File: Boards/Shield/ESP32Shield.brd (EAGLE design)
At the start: 58.4 x 25.4 mm, 28 parts, among them Q1 220mA/50V/3.5Ω, U1 5V

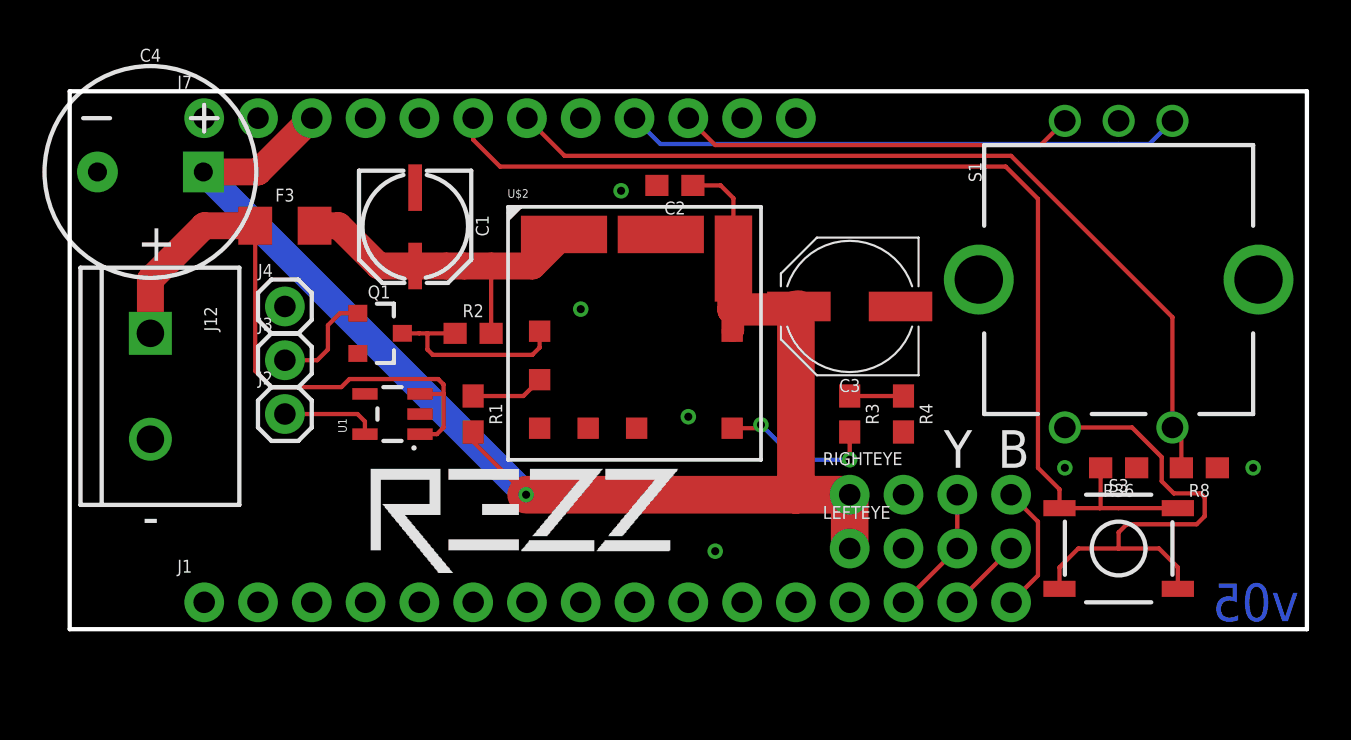
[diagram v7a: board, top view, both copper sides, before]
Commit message: updating board to V06, finangling code to work with WROOM
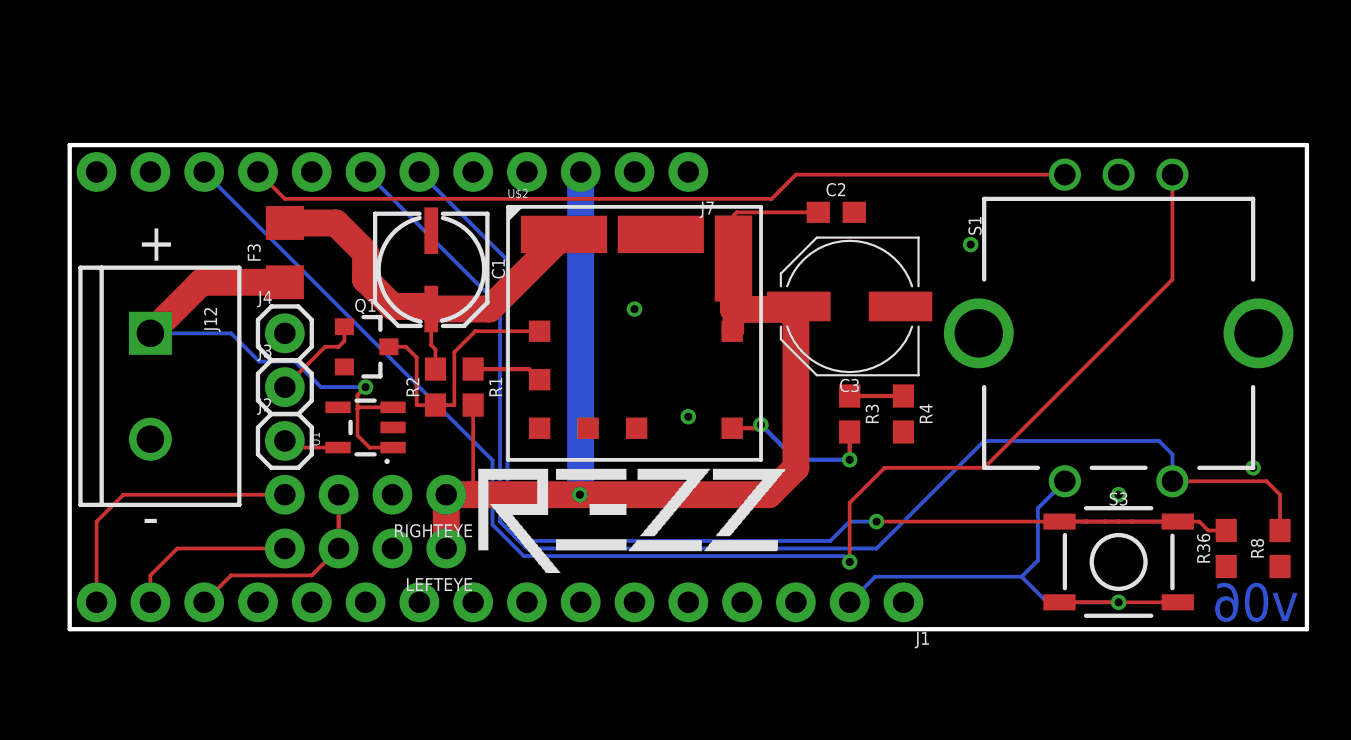
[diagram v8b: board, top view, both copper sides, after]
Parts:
- removed C4: 1mF, SparkFun-Capacitors:CPOL-RADIAL-5MM-10MM
- moved J1 33.0 mm to (39.4, 1.27), turned to 180 degrees
- moved J7 23.0 mm to (29.2, 21.6), turned to 180 degrees
- moved LEFTEYE 19.0 mm to (17.8, 3.81), turned to 180 degrees
- moved RIGHTEYE 19.0 mm to (17.8, 6.35), turned to 180 degrees
- moved C2 7.73 mm to (36.2, 19.7), turned to 0 degrees
- moved R36 6.35 mm to (54.6, 3.81), turned to 90 degrees
- moved R8 5.39 mm to (57.1, 3.81), turned to 90 degrees
- moved U$1 5.08 mm to (26.6, 5.11)
- moved R2 3.10 mm to (17.3, 11.4), turned to 90 degrees
- moved U$4 2.79 mm to (49.5, 17.7)
- moved S1 2.54 mm to (49.5, 14.0)
- moved U$3 2.54 mm to (49.4, 9.91)
- moved C1 2.17 mm to (17.3, 17.0)
- moved U1 1.42 mm to (14.0, 9.53)
- moved F3 1.27 mm to (10.2, 17.8), turned to 90 degrees
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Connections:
- removed net 14/ENC-B: J7.10, S1.B
- removed net 32/ENC-A: J7.9, S1.A
- removed net 3V3: J1.2
- new net 14/ENC-A: J7.10, S1.A
- new net 32/ENC-B: J7.9, S1.B
- net 3.3V: now also J1.2
- net 5V: no longer C4.+
- net GND: no longer C4.-
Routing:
- net 14/ENC-A: track 0.00 -> 67.2 mm, vias 0 -> 1
- net 32/ENC-B: track 0.00 -> 39.1 mm
- net 32/ENC-A: track 26.4 -> 0.00 mm
- net 33/BTN2: track 41.7 -> 62.1 mm
- net 14/ENC-B: track 18.8 -> 0.00 mm
- net 5V: track 72.3 -> 61.7 mm
- net 23/DL: track 6.13 -> 13.2 mm
- net VBATT: track 29.3 -> 24.6 mm, vias 0 -> 1
- net 17/DR: track 3.59 -> 8.15 mm
- net 16/CLOCK: track 6.13 -> 9.94 mm
- net N$2: track 16.4 -> 20.0 mm
- net N$3: track 9.57 -> 12.5 mm
- net POWER_CONTROL: track 4.52 -> 2.64 mm
- net 27/BTN1: track 51.4 -> 53.0 mm, vias 0 -> 1
- net 3.3V: track 23.0 -> 24.6 mm, vias 0 -> 1
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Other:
- board size 58.4 x 25.4 mm -> 58.4 x 22.9 mm
- board text added: "v06"
- board text removed: "B"
- board text removed: "Y"
- board text removed: "v05"
